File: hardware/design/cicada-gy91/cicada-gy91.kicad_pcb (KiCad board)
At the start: 2 copper layers, 36.8 x 21.6 mm, 5 parts, among them J1 Expansion slot1, J2 Expansion slot2, J3 GY-91 Module

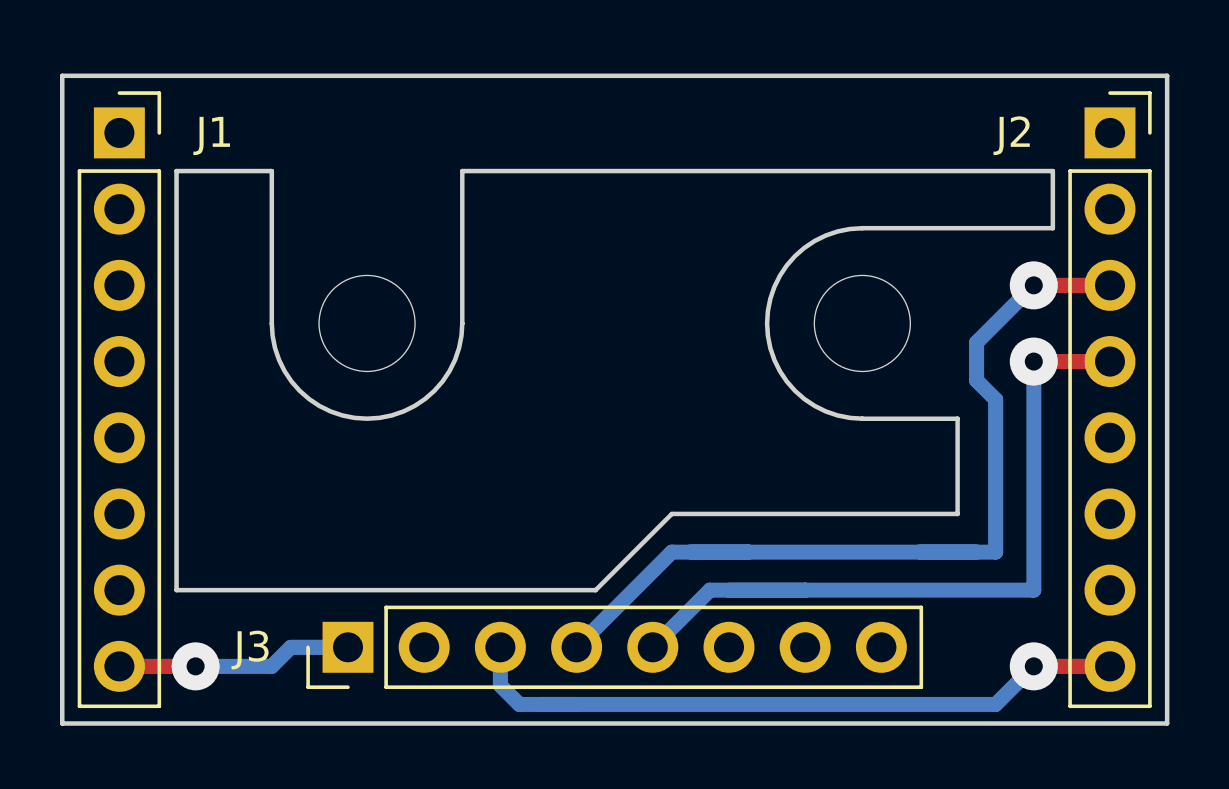
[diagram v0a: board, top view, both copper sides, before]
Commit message: added new board cicada-gy91-v3
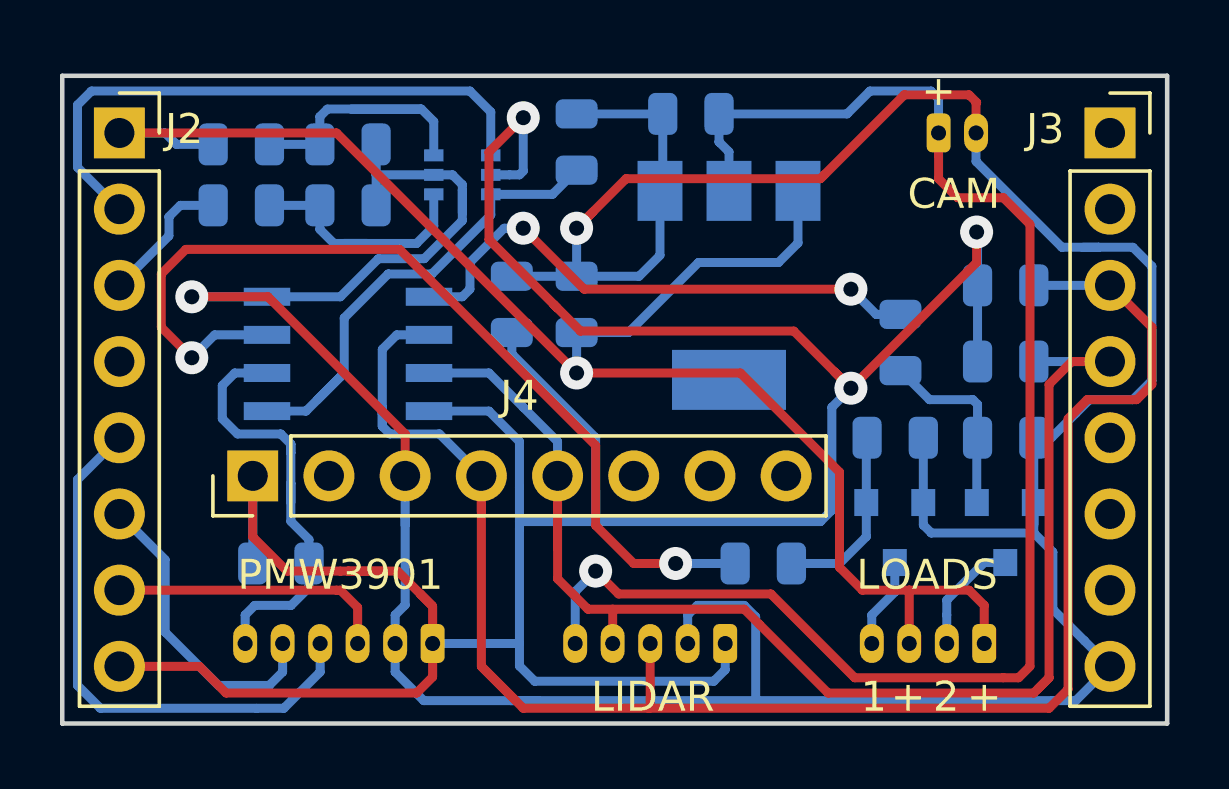
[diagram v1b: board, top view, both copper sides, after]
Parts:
- removed REF** (x2): MountingHole_3.2mm_M3, MountingHole:MountingHole_3.2mm_M3
- added C1: 100 nF, Capacitor_SMD:C_0805_2012Metric, B.Cu at (144.5, 97.8)
- added C2: 10uF, Capacitor_SMD:C_0805_2012Metric, B.Cu at (150.5, 91.4)
- added C3: 10uF, Capacitor_SMD:C_0805_2012Metric, B.Cu at (146.7, 97.8)
- added J1: LOADS, Connector_Molex:Molex_PicoBlade_53048-0810_1x04_P1.25mm_Horizontal, B.Cu at (160.3, 109.1)
- added J5: Lidar, Connector_Molex:Molex_PicoBlade_53048-1010_1x05_P1.25mm_Horizontal, B.Cu at (151.6, 109.1)
- added J6: PMW3901, Connector_Molex:Molex_PicoBlade_53048-1210_1x06_P1.25mm_Horizontal, B.Cu at (141.9, 109.1)
- added J7: CAM, Connector_Molex:Molex_PicoBlade_53048-0410_1x02_P1.25mm_Horizontal, B.Cu at (158.8, 92.1)
- added Q1: IRLML2502, Package_TO_SOT_SMD:SOT-23, B.Cu at (161.0, 105.4)
- added Q2: IRLML2502, Package_TO_SOT_SMD:SOT-23, B.Cu at (157.3, 105.4)
- added R1: 82k, Resistor_SMD:R_0805_2012Metric, B.Cu at (135.5, 94.5)
- added R10: 1k, Resistor_SMD:R_0805_2012Metric, B.Cu at (152.9, 106.4)
- added R11: 3k3, Resistor_SMD:R_0805_2012Metric, B.Cu at (161.0, 97.2)
- added R12: 3k3, Resistor_SMD:R_0805_2012Metric, B.Cu at (161.0, 99.7)
- added R2: 30k, Resistor_SMD:R_0805_2012Metric, B.Cu at (139.1, 94.5)
- added R3: 390k, Resistor_SMD:R_0805_2012Metric, B.Cu at (135.5, 92.5)
- added R4: 30k, Resistor_SMD:R_0805_2012Metric, B.Cu at (139.1, 92.5)
- added R5: 30k, Resistor_SMD:R_0805_2012Metric, B.Cu at (136.8, 106.4)
- added R6: 30k, Resistor_SMD:R_0805_2012Metric, B.Cu at (146.7, 92.4)
- added R7: 30k, Resistor_SMD:R_0805_2012Metric, B.Cu at (161.0, 102.2)
- added R8: 30k, Resistor_SMD:R_0805_2012Metric, B.Cu at (157.3, 102.2)
- added R9: 1k, Resistor_SMD:R_0805_2012Metric, B.Cu at (157.5, 99.1)
- added U1: 74LVC1G3157, Package_TO_SOT_SMD:SOT-363_SC-70-6, B.Cu at (142.9, 93.5)
- added U2: PCA9536D, Package_SO:SOIC-8_3.9x4.9mm_P1.27mm, B.Cu at (139.1, 99.4)
- added U3: LM1117-3.3, Package_TO_SOT_SMD:SOT-223, B.Cu at (151.8, 97.2)
- moved J4 6.54 mm to (135.9, 103.5)
- renumbered J1 to J2, J2 to J3, J3 to J4
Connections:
- net /3V3 renamed +3V3
- net /CSB renamed Net-(J4-Pad8)
- net /GND renamed GND
- net /M1 renamed Net-(J3-Pad7)
- net /M2 renamed Net-(J3-Pad6)
- net /M3 renamed Net-(J3-Pad5)
- net /M4 renamed Net-(J2-Pad4)
- net /NCS renamed Net-(J4-Pad7)
- net /RXD renamed Net-(J3-Pad2)
- net /SA0 renamed Net-(J4-Pad6)
- net /TXD renamed Net-(J3-Pad1)
- J2 pad 1: /+BATT -> +BATT
- J2 pad 3: /+5V -> /CURN
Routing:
- net GND: track 23.6 -> 131.8 mm, vias 1 -> 2
- net +3V3: track 7.88 -> 105.8 mm, vias 1 -> 3
- net +BATT: track 0.00 -> 55.2 mm, vias 0 -> 1
- net APWR: track 0.00 -> 50.3 mm, vias 0 -> 1
- net /LOAD1: track 0.00 -> 31.4 mm, vias 0 -> 2
- net /SCL: track 31.6 -> 59.6 mm, vias 1 -> 0
- net /SDA: track 26.2 -> 46.5 mm, vias 1 -> 0
- net /ADC: track 0.00 -> 19.8 mm
- net /SCK: track 0.00 -> 18.7 mm
- net /LOAD2: track 0.00 -> 18.4 mm, vias 0 -> 2
- net /ADC_CH: track 0.00 -> 16.2 mm
- net /CS1: track 0.00 -> 15.1 mm
- net /MISO: track 0.00 -> 10.4 mm
- net Net-(R3-Pad2): track 0.00 -> 10.1 mm
- net /MOSI: track 0.00 -> 9.38 mm
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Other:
- outline, holes or cut-outs redrawn
- net class Default: clearance 0.3 -> 0.2; trace_width 0.5 -> 0.3; via_dia 1.6 -> 1.1; via_drill 0.6 -> 0.5
- rule trace_clearance: 0.3 -> 0.2
- rule trace_min: 0.2 -> 0.3
- board text added: "+"
- board text added: "1"
- board text added: "2"
- board text added: "CAM"
- board text added: "LIDAR"
- board text added: "LOADS"
- board text added: "PMW3901"
